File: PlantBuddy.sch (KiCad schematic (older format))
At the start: 30 parts, among them J101 J-Link SWD, Q101 AO3401A, U101 nRF52832-QFxx, U102 LTR-303ALS-01, U6 SHTC3, Y1 32MHz, Y2 32kHz

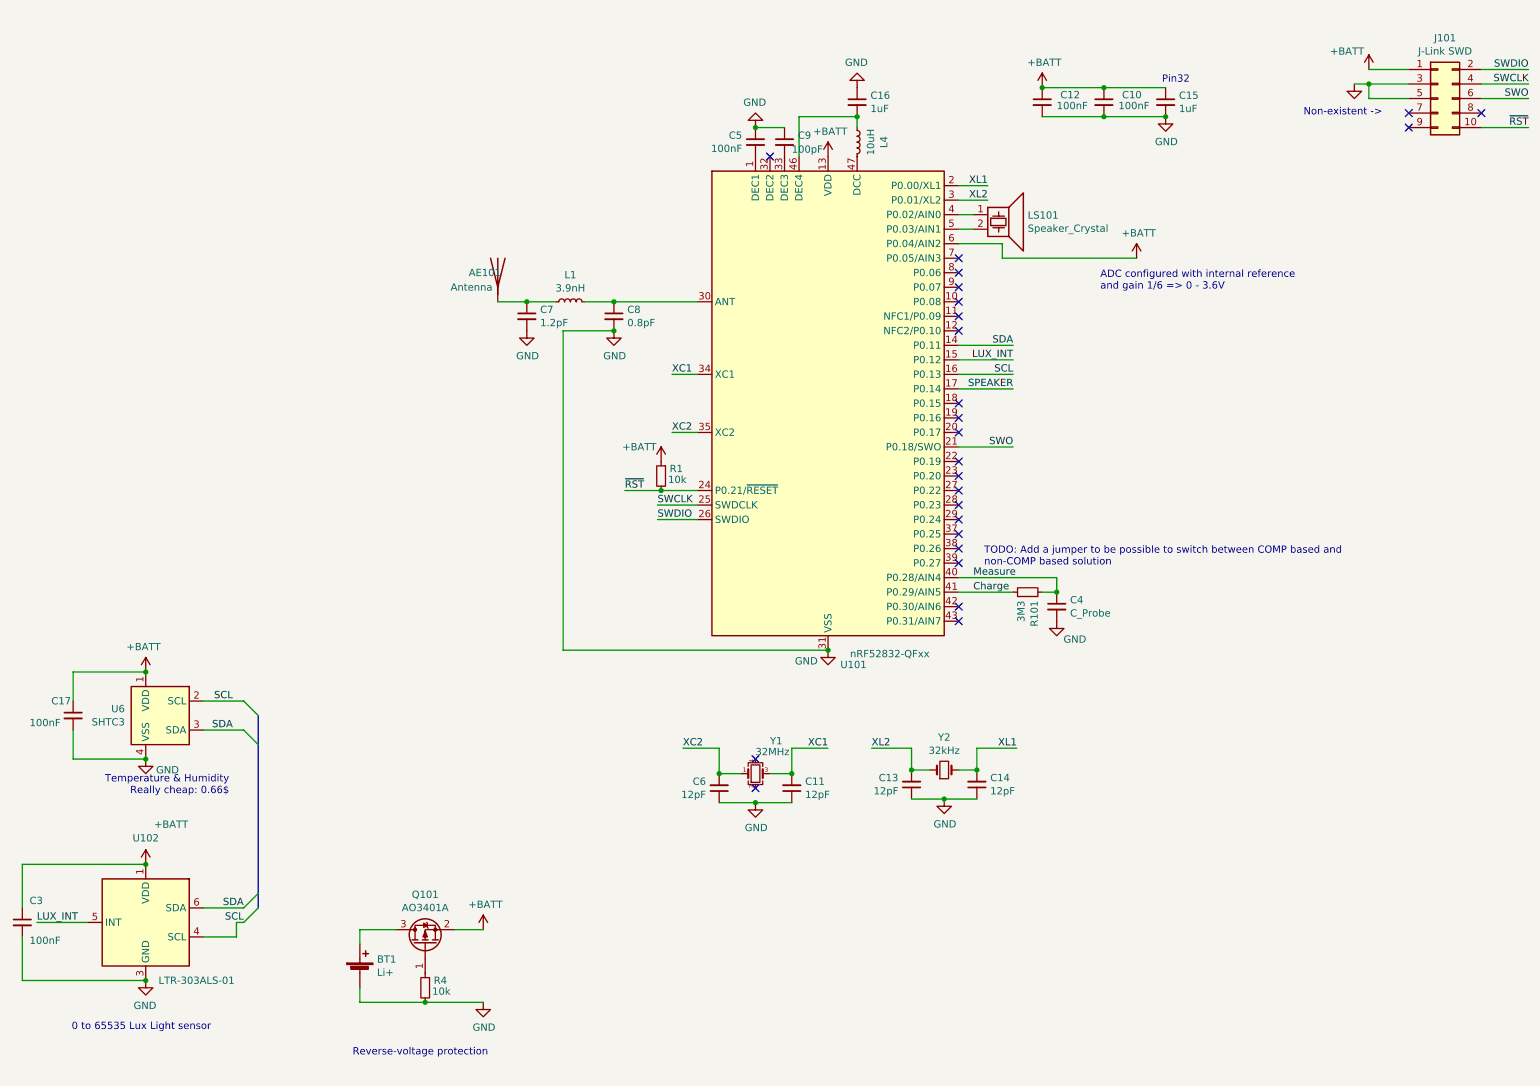
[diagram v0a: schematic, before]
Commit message: Added current sense resistor & COMP resistor.
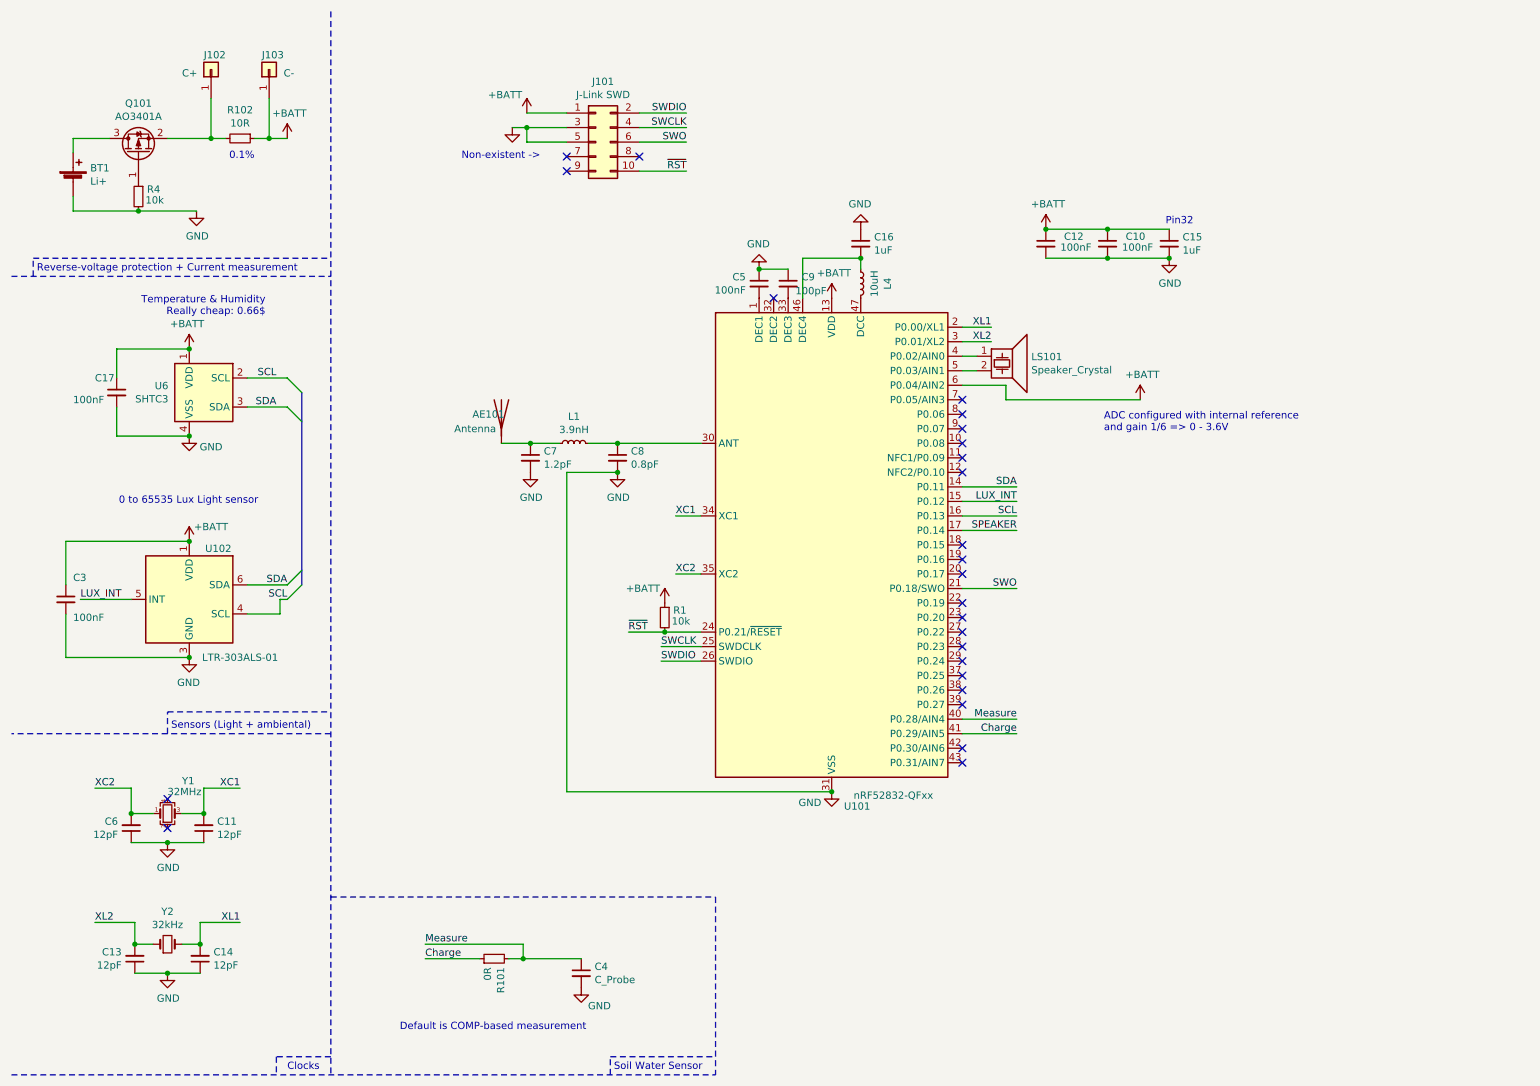
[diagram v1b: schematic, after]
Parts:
- added J102: C+, TestPoint:TestPoint_Pad_1.5x1.5mm, symbol Connector_Generic:Conn_01x01
- added J103: C-, TestPoint:TestPoint_Pad_1.5x1.5mm, symbol Connector_Generic:Conn_01x01
- added R102: 10R, Resistor_SMD:R_0603_1608Metric, symbol Device:R_Small
- R101: value 3M3 -> 0R
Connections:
- net +BATT: now also J103.1 (Pin_1), R102.1; no longer Q101.2 (S)
- new net: J102.1 (Pin_1), Q101.2 (S), R102.2
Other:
- note added: "0.1%"
- note added: "Clocks"
- note added: "Default is COMP-based measurement"
- note added: "Reverse-voltage protection + Current measurement"
- note added: "Sensors (Light + ambiental)"
- note added: "Soil Water Sensor"
- note removed: "Reverse-voltage protection"
- note removed: "TODO: Add a jumper to be possible to switch between COMP based and\nnon-COMP based solution"
- moved on the sheet: AE101, BT1, C10, C11, C12, C13, C14, C15, C16, C17, C3, C4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
